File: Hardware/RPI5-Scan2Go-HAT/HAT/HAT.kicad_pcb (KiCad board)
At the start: 2 copper layers, 65 x 56.5 mm, 7 parts, among them J1 RPi_GPIO, J2 RPi_GPIO, U1 Pico

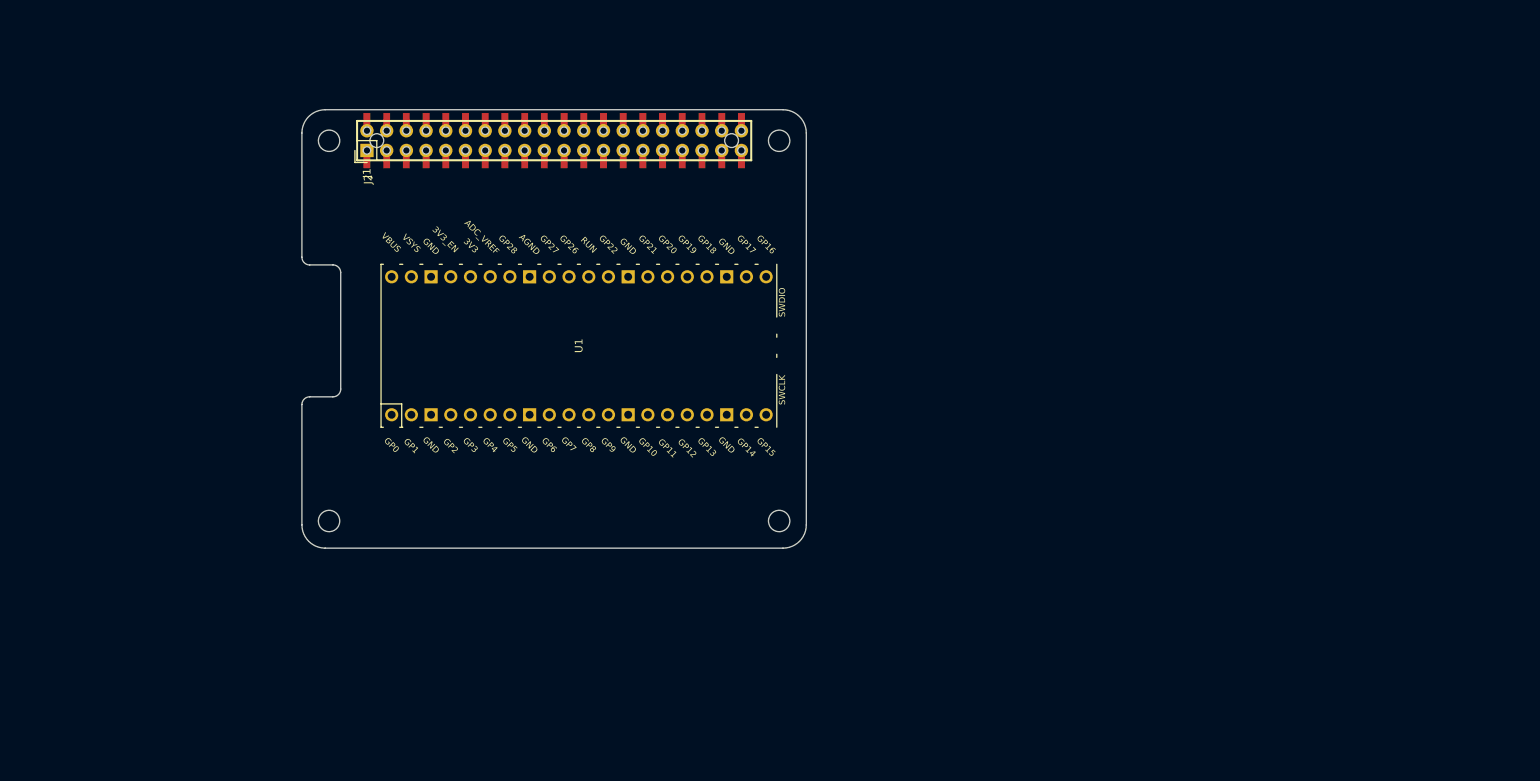
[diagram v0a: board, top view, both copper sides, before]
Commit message: created footprint for Adafruit amplifier
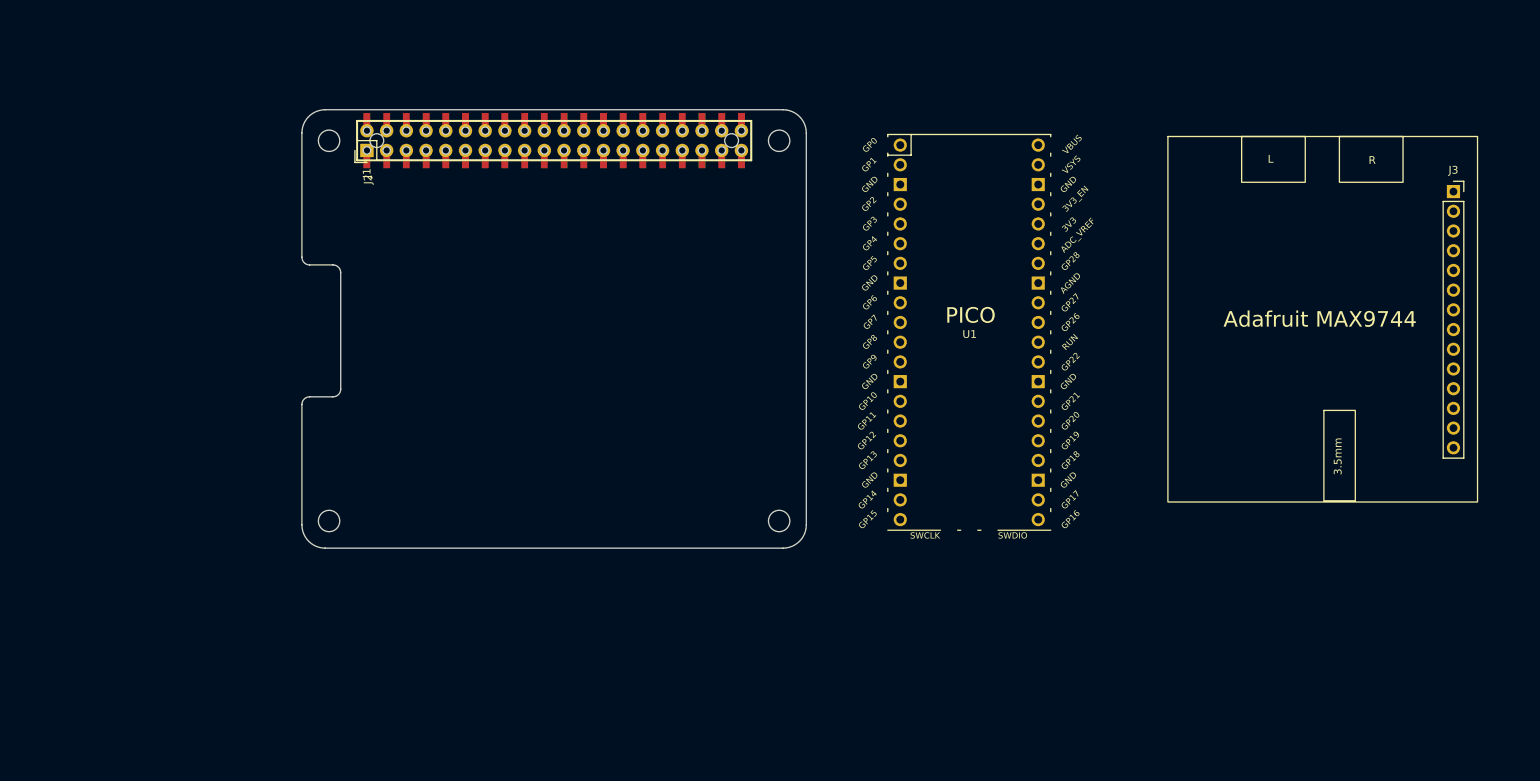
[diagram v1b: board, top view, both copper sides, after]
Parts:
- added J3: Conn_01x14_Socket, Connector_PinSocket_2.54mm:PinSocket_1x14_P2.54mm_Vertical, F.Cu at (255.9, 74.5)
- moved U1 50.3 mm to (193.5, 92.7), turned to 0 degrees

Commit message: started pcb routing
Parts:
- removed J2: RPi_GPIO, _custom:Samtec_HLE-120-02-XXX-DV-BE-XX-XX
- moved J3 134.1 mm to (123.4, 95.2), turned to 90 degrees
- moved U1 56.6 mm to (138.1, 81.4), turned to 90 degrees
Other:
- board text added: "GND"
- board text added: "GP0"
- board text added: "GP1"
- board text added: "GP10"
- board text added: "GP11"
- board text added: "GP12"
- board text added: "GP13"
- board text added: "GP14"
- board text added: "GP15"
- board text added: "GP2"
- board text added: "GP3"
- board text added: "GP4"
- board text added: "GP5"
- board text added: "GP6"
- board text added: "GP7"
- board text added: "GP8"
- board text added: "GP9"

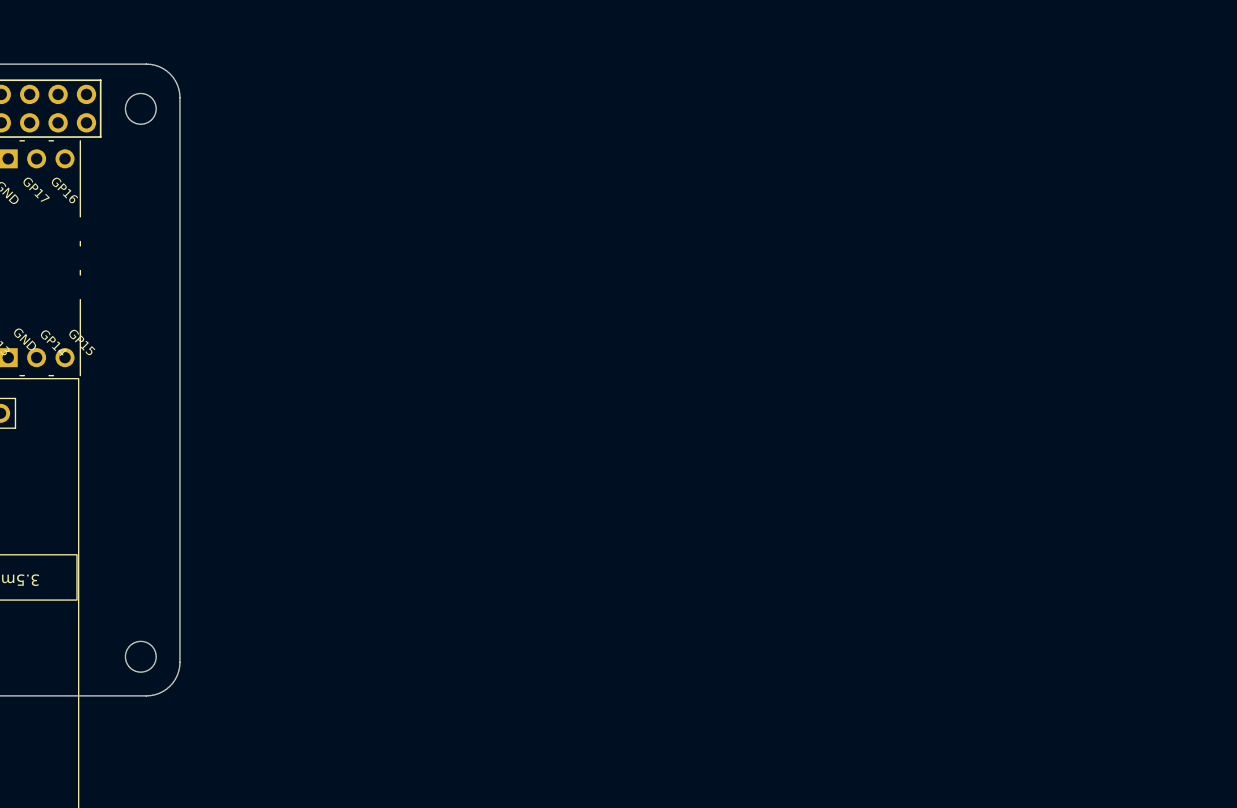
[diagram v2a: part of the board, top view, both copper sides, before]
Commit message: added doxygen compatible comments to main
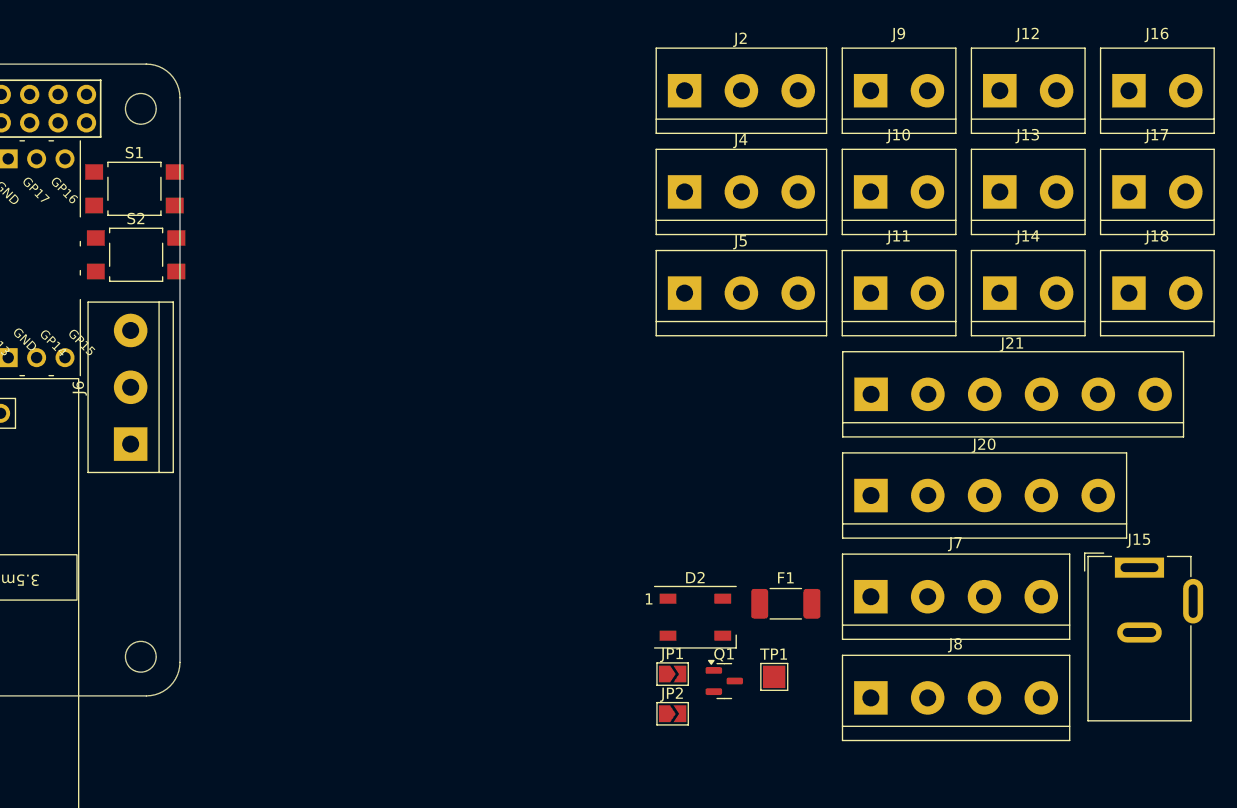
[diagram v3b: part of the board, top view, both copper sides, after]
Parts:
- added D2: WS2812B, LED_SMD:LED_WS2812B_PLCC4_5.0x5.0mm_P3.2mm, F.Cu at (218.6, 113.5)
- added F1: 6A, Fuse:Fuse_2010_5025Metric_Pad1.52x2.65mm_HandSolder, F.Cu at (226.7, 112.3)
- added J10: Screw_Terminal_01x02, TerminalBlock:TerminalBlock_bornier-2_P5.08mm, F.Cu at (234.3, 75.4)
- added J11: Screw_Terminal_01x02, TerminalBlock:TerminalBlock_bornier-2_P5.08mm, F.Cu at (234.3, 84.5)
- added J12: Screw_Terminal_01x02, TerminalBlock:TerminalBlock_bornier-2_P5.08mm, F.Cu at (245.8, 66.4)
- added J13: Screw_Terminal_01x02, TerminalBlock:TerminalBlock_bornier-2_P5.08mm, F.Cu at (245.8, 75.4)
- added J14: Screw_Terminal_01x02, TerminalBlock:TerminalBlock_bornier-2_P5.08mm, F.Cu at (245.8, 84.5)
- added J15: Jack-DC 5V, Connector_BarrelJack:BarrelJack_Wuerth_6941xx301002, F.Cu at (258.3, 109.0)
- added J16: Screw_Terminal_01x02, TerminalBlock:TerminalBlock_bornier-2_P5.08mm, F.Cu at (257.4, 66.4)
- added J17: Screw_Terminal_01x02, TerminalBlock:TerminalBlock_bornier-2_P5.08mm, F.Cu at (257.4, 75.4)
- added J18: Screw_Terminal_01x02, TerminalBlock:TerminalBlock_bornier-2_P5.08mm, F.Cu at (257.4, 84.5)
- added J2: Screw_Terminal_01x03, TerminalBlock:TerminalBlock_bornier-3_P5.08mm, F.Cu at (217.6, 66.4)
- added J20: Screw_Terminal_01x05, TerminalBlock:TerminalBlock_bornier-5_P5.08mm, F.Cu at (234.3, 102.6)
- added J21: Screw_Terminal_01x06, TerminalBlock:TerminalBlock_bornier-6_P5.08mm, F.Cu at (234.3, 93.5)
- added J4: Screw_Terminal_01x03, TerminalBlock:TerminalBlock_bornier-3_P5.08mm, F.Cu at (217.6, 75.4)
- added J5: Screw_Terminal_01x03, TerminalBlock:TerminalBlock_bornier-3_P5.08mm, F.Cu at (217.6, 84.5)
- added J6: Screw_Terminal_01x03, TerminalBlock:TerminalBlock_bornier-3_P5.08mm, F.Cu at (168.1, 98.0)
- added J7: Screw_Terminal_01x04, TerminalBlock:TerminalBlock_bornier-4_P5.08mm, F.Cu at (234.3, 111.6)
- added J8: Screw_Terminal_01x04, TerminalBlock:TerminalBlock_bornier-4_P5.08mm, F.Cu at (234.3, 120.7)
- added J9: Screw_Terminal_01x02, TerminalBlock:TerminalBlock_bornier-2_P5.08mm, F.Cu at (234.3, 66.4)
- added JP1: Jumper_2_Open, Jumper:SolderJumper-2_P1.3mm_Open_TrianglePad1.0x1.5mm, F.Cu at (216.6, 118.5)
- added JP2: Jumper_2_Open, Jumper:SolderJumper-2_P1.3mm_Open_TrianglePad1.0x1.5mm, F.Cu at (216.6, 122.1)
- added Q1: DMG2305UX, Package_TO_SOT_SMD:SOT-23, F.Cu at (221.2, 119.2)
- added S1: MOMENTARY-SWITCH-SPST-2-SMD-5.2MM, Button_Switch_SMD:SW_SPST_TL3305B, F.Cu at (168.4, 75.2)
- added S2: MOMENTARY-SWITCH-SPST-2-SMD-5.2MM, Button_Switch_SMD:SW_SPST_TL3305B, F.Cu at (168.6, 81.0)
- added TP1: TestPoint, TestPoint:TestPoint_Pad_2.0x2.0mm, F.Cu at (225.7, 118.8)
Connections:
- J1 pad 1: Net-(J1-3.3V-Pad1) -> unconnected-(J1-3.3V-Pad1)
- J1 pad 10: Net-(J1-BCM15_RXD) -> unconnected-(J1-BCM15_RXD-Pad10)
- J1 pad 13: Net-(J1-BCM27) -> unconnected-(J1-BCM27-Pad13)
- J1 pad 14: Net-(J1-GND-Pad14) -> GND
- J1 pad 15: Net-(J1-BCM22) -> unconnected-(J1-BCM22-Pad15)
- J1 pad 16: Net-(J1-BCM23) -> unconnected-(J1-BCM23-Pad16)
- J1 pad 17: Net-(J1-3.3V-Pad17) -> unconnected-(J1-3.3V-Pad17)
- J1 pad 18: Net-(J1-BCM24) -> unconnected-(J1-BCM24-Pad18)
- J1 pad 19: Net-(J1-BCM10_MOSI) -> unconnected-(J1-BCM10_MOSI-Pad19)
- J1 pad 2: Net-(J1-5V-Pad2) -> +5V
- J1 pad 20: Net-(J1-GND-Pad20) -> unconnected-(J1-GND-Pad20)
- J1 pad 21: Net-(J1-BCM9_MISO) -> unconnected-(J1-BCM9_MISO-Pad21)
- J1 pad 22: Net-(J1-BCM25) -> unconnected-(J1-BCM25-Pad22)
- J1 pad 23: Net-(J1-BCM11_SCLK) -> unconnected-(J1-BCM11_SCLK-Pad23)
- J1 pad 24: Net-(J1-BCM8_CE0) -> unconnected-(J1-BCM8_CE0-Pad24)
- J1 pad 25: Net-(J1-GND-Pad25) -> GND
- J1 pad 26: Net-(J1-BCM7_CE1) -> unconnected-(J1-BCM7_CE1-Pad26)
- J1 pad 27: Net-(J1-BCM0_ID_SD) -> unconnected-(J1-BCM0_ID_SD-Pad27)
- J1 pad 28: Net-(J1-BCM1_ID_SC) -> unconnected-(J1-BCM1_ID_SC-Pad28)
- J1 pad 29: Net-(J1-BCM5) -> unconnected-(J1-BCM5-Pad29)
- J1 pad 30: Net-(J1-GND-Pad30) -> GND
- J1 pad 31: Net-(J1-BCM6) -> unconnected-(J1-BCM6-Pad31)
- J1 pad 33: Net-(J1-BCM13_PWM1) -> unconnected-(J1-BCM13_PWM1-Pad33)
- J1 pad 34: Net-(J1-GND-Pad34) -> unconnected-(J1-GND-Pad34)
- J1 pad 35: Net-(J1-BCM19_MISO_PCM_FS) -> unconnected-(J1-BCM19_MISO_PCM_FS-Pad35)
- J1 pad 36: Net-(J1-BCM16) -> unconnected-(J1-BCM16-Pad36)
- J1 pad 37: Net-(J1-BCM26) -> unconnected-(J1-BCM26-Pad37)
- J1 pad 38: Net-(J1-BCM20_MOSI_PCM_DI) -> unconnected-(J1-BCM20_MOSI_PCM_DI-Pad38)
- J1 pad 39: Net-(J1-GND-Pad39) -> GND
- J1 pad 4: Net-(J1-5V-Pad4) -> +5V
- J1 pad 40: Net-(J1-BCM21_SCLK_PCM_DO) -> unconnected-(J1-BCM21_SCLK_PCM_DO-Pad40)
- J1 pad 6: Net-(J1-GND-Pad6) -> GND
- J1 pad 7: Net-(J1-BCM4_GPCLK0) -> unconnected-(J1-BCM4_GPCLK0-Pad7)
- J1 pad 8: Net-(J1-BCM14_TXD) -> unconnected-(J1-BCM14_TXD-Pad8)
- J1 pad 9: Net-(J1-GND-Pad9) -> GND
- J3 pad 1: unconnected-(J3-VDD-Pad1) -> +5V
- J3 pad 10: unconnected-(J3-SCL-Pad10) -> Net-(J1-BCM3_SCL)
- J3 pad 11: unconnected-(J3-SDA-Pad11) -> Net-(J1-BCM2_SDA)
- J3 pad 13: unconnected-(J3-LIN-Pad13) -> Net-(J3-LIN)
- J3 pad 14: unconnected-(J3-RIN-Pad14) -> Net-(J3-RIN)
- J3 pad 2: unconnected-(J3-GND-Pad2) -> GND
- J3 pad 7: unconnected-(J3-MUTE-Pad7) -> Net-(J1-BCM17)
- U1 pad 1: unconnected-(U1-GPIO0-Pad1) -> Net-(J8-Pin_3)
- U1 pad 10: unconnected-(U1-GPIO7-Pad10) -> Net-(J2-Pin_3)
- U1 pad 11: unconnected-(U1-GPIO8-Pad11) -> Net-(J2-Pin_2)
- U1 pad 12: unconnected-(U1-GPIO9-Pad12) -> Net-(J2-Pin_1)
- U1 pad 13: unconnected-(U1-GND-Pad13) -> GND
- U1 pad 14: unconnected-(U1-GPIO10-Pad14) -> Net-(J9-Pin_2)
- U1 pad 15: unconnected-(U1-GPIO11-Pad15) -> Net-(J12-Pin_2)
- U1 pad 16: unconnected-(U1-GPIO12-Pad16) -> Net-(J13-Pin_2)
- U1 pad 17: unconnected-(U1-GPIO13-Pad17) -> Net-(J14-Pin_2)
- U1 pad 18: unconnected-(U1-GND-Pad18) -> GND
- U1 pad 19: unconnected-(U1-GPIO14-Pad19) -> Net-(J18-Pin_2)
- U1 pad 2: unconnected-(U1-GPIO1-Pad2) -> Net-(J8-Pin_2)
- U1 pad 20: unconnected-(U1-GPIO15-Pad20) -> Net-(J18-Pin_1)
- U1 pad 21: unconnected-(U1-GPIO16-Pad21) -> Net-(J10-Pin_2)
- U1 pad 22: unconnected-(U1-GPIO17-Pad22) -> Net-(J11-Pin_2)
- U1 pad 23: unconnected-(U1-GND-Pad23) -> GND
- U1 pad 24: unconnected-(U1-GPIO18-Pad24) -> Net-(J16-Pin_2)
- U1 pad 25: unconnected-(U1-GPIO19-Pad25) -> Net-(J17-Pin_2)
- U1 pad 26: unconnected-(U1-GPIO20-Pad26) -> Net-(D2-DIN)
- U1 pad 27: unconnected-(U1-GPIO21-Pad27) -> Net-(U1-GPIO21)
- U1 pad 28: unconnected-(U1-GND-Pad28) -> GND
- U1 pad 3: unconnected-(U1-GND-Pad3) -> GND
- U1 pad 30: unconnected-(U1-RUN-Pad30) -> Net-(U1-RUN)
- U1 pad 31: unconnected-(U1-GPIO26_ADC0-Pad31) -> Net-(J20-Pin_5)
- U1 pad 32: unconnected-(U1-GPIO27_ADC1-Pad32) -> Net-(J20-Pin_4)
- U1 pad 33: unconnected-(U1-AGND-Pad33) -> Net-(J20-Pin_3)
- U1 pad 34: unconnected-(U1-GPIO28_ADC2-Pad34) -> Net-(J20-Pin_2)
- U1 pad 35: unconnected-(U1-ADC_VREF-Pad35) -> Net-(J20-Pin_1)
- U1 pad 36: unconnected-(U1-3V3-Pad36) -> Net-(J21-Pin_4)
- U1 pad 38: unconnected-(U1-GND-Pad38) -> GND
- U1 pad 39: unconnected-(U1-VSYS-Pad39) -> Net-(Q1-S)
- U1 pad 4: unconnected-(U1-GPIO2-Pad4) -> Net-(J4-Pin_2)
- U1 pad 40: unconnected-(U1-VBUS-Pad40) -> Net-(Q1-G)
- U1 pad 5: unconnected-(U1-GPIO3-Pad5) -> Net-(J5-Pin_2)
- U1 pad 6: unconnected-(U1-GPIO4-Pad6) -> Net-(J7-Pin_3)
- U1 pad 7: unconnected-(U1-GPIO5-Pad7) -> Net-(J7-Pin_2)
- U1 pad 8: unconnected-(U1-GND-Pad8) -> GND
- U1 pad 9: unconnected-(U1-GPIO6-Pad9) -> Net-(J6-Pin_2)
